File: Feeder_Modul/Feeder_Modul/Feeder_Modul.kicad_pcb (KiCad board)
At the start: 2 copper layers, 156.6 x 125.2 mm, 101 parts, among them J1 Conn_02x01, J101 Conn_02x01, J102 Conn_01x06_Male, J103 Conn_02x01, J104 Conn_02x01, J105 Conn_02x01, J106 WE_629104190121, J107 Conn_02x07_Odd_Even, J108 Conn_02x01, J109 Conn_02x01, SW101 SW_Push, SW102 SW_Push, SW103 SW_Push, SW104 SW_Push, SW105 SW_Push, U1 TPS560430, U101 TPS560430, U102 STM32F105R8Tx, U103 M24C01-WMN, U104 TCST5250, U105 DRV8835, U106 Panasonic_ESE22, U107 SN65HVD230, U108 N20_DC_Motor, U109 N20_DC_Motor, Y101 48MHz

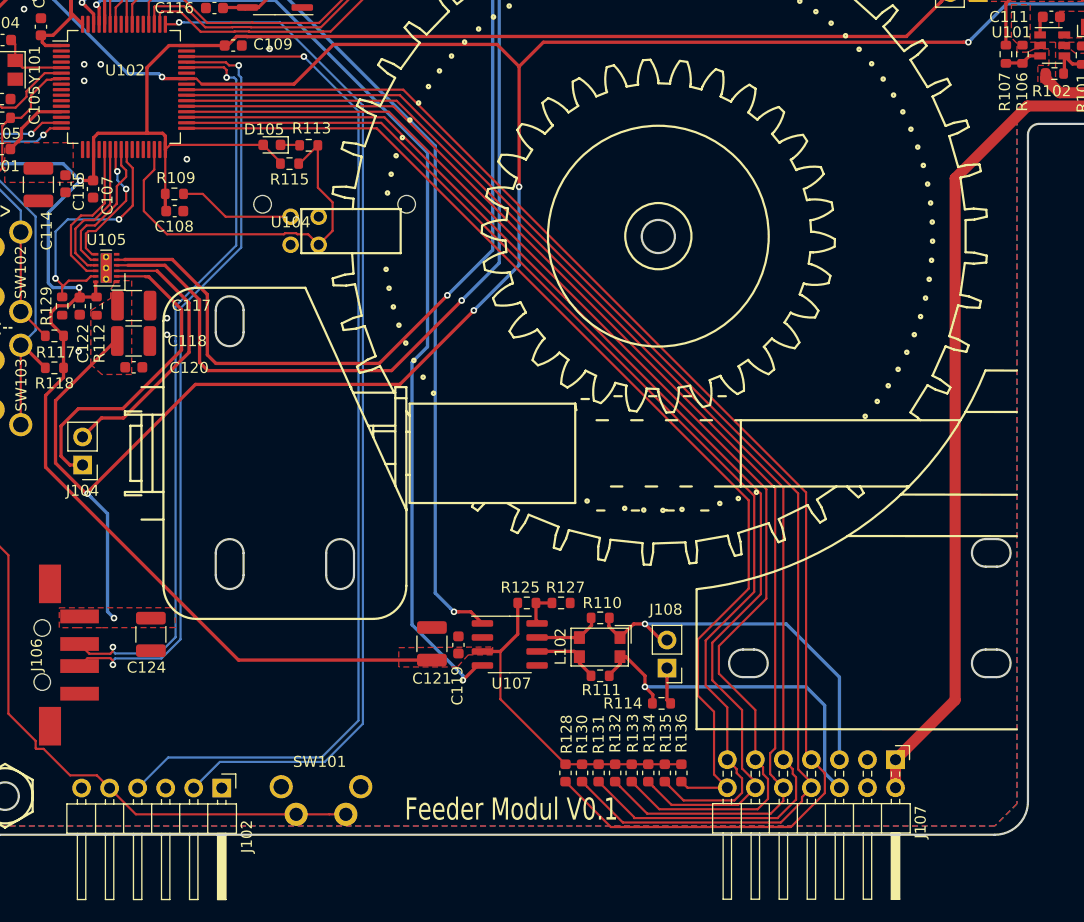
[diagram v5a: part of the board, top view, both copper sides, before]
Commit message: Feeder Rails hinzugefügt
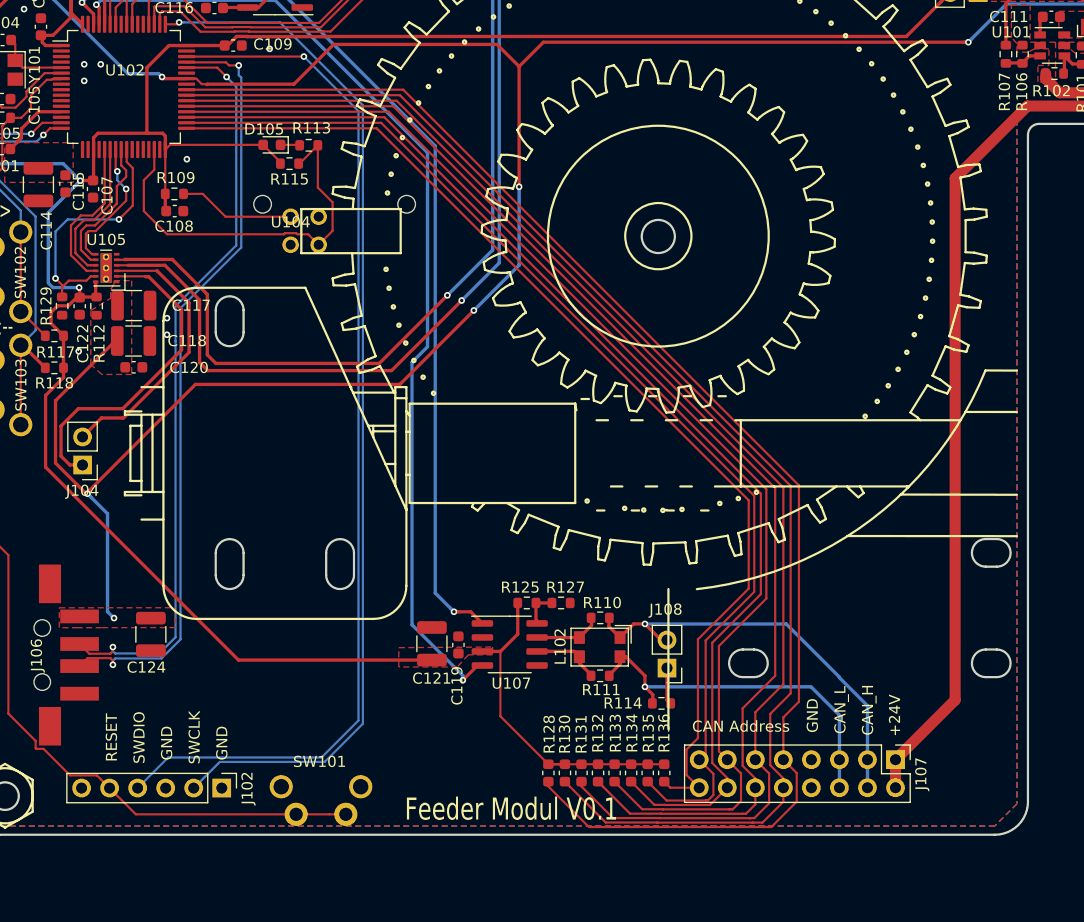
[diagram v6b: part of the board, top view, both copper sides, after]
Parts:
- J102: footprint Connector_PinHeader_2.54mm:PinHeader_1x06_P2.54mm_Horizontal -> Connector_PinHeader_2.54mm:PinHeader_1x06_P2.54mm_Vertical
- J107: footprint Connector_PinHeader_2.54mm:PinHeader_2x07_P2.54mm_Horizontal -> Connector_PinHeader_2.54mm:PinHeader_2x08_P2.54mm_Vertical
- moved R128 1.55 mm to (116.5, 155.2)
- moved R130 1.55 mm to (118.0, 155.2)
- moved R131 1.55 mm to (119.5, 155.2)
- moved R132 1.55 mm to (121.0, 155.2)
- moved R133 1.55 mm to (122.5, 155.2)
- moved R134 1.55 mm to (124.0, 155.2)
- moved R135 1.55 mm to (125.5, 155.2)
- moved R136 1.55 mm to (127.0, 155.2)
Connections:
- J107 pad 10: /ADDR3 -> /ADDR1
- J107 pad 11: /ADDR4 -> /ADDR2
- J107 pad 12: /ADDR5 -> /ADDR3
- J107 pad 13: /ADDR6 -> /ADDR4
- J107 pad 14: /ADDR7 -> /ADDR5
- J107 pad 3: GND -> /CAN1_H
- J107 pad 4: GND -> /CAN1_H
- J107 pad 5: /CAN1_H -> /CAN1_L
- J107 pad 7: /ADDR0 -> GND
- J107 pad 8: /ADDR1 -> GND
- J107 pad 9: /ADDR2 -> /ADDR0
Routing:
- net /CAN1_H: track 34.7 -> 38.3 mm
- net /ADDR5: track 107.4 -> 105.4 mm
- net /ADDR4: track 112.1 -> 110.3 mm
- net /ADDR6: track 103.5 -> 102.0 mm
- net /ADDR7: track 98.3 -> 97.1 mm
- net +3V3: track 350.6 -> 351.5 mm
- net /USB_OTG-: track 68.8 -> 68.0 mm
- net /ADDR2: track 117.3 -> 117.9 mm
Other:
- rule trace_min: 0.1 -> 0.15
- board text added: "+24V"
- board text added: "CAN Address"
- board text added: "CAN_H"
- board text added: "CAN_L"
- board text added: "GND"
- board text added: "RESET"
- board text added: "SWCLK"
- board text added: "SWDIO"

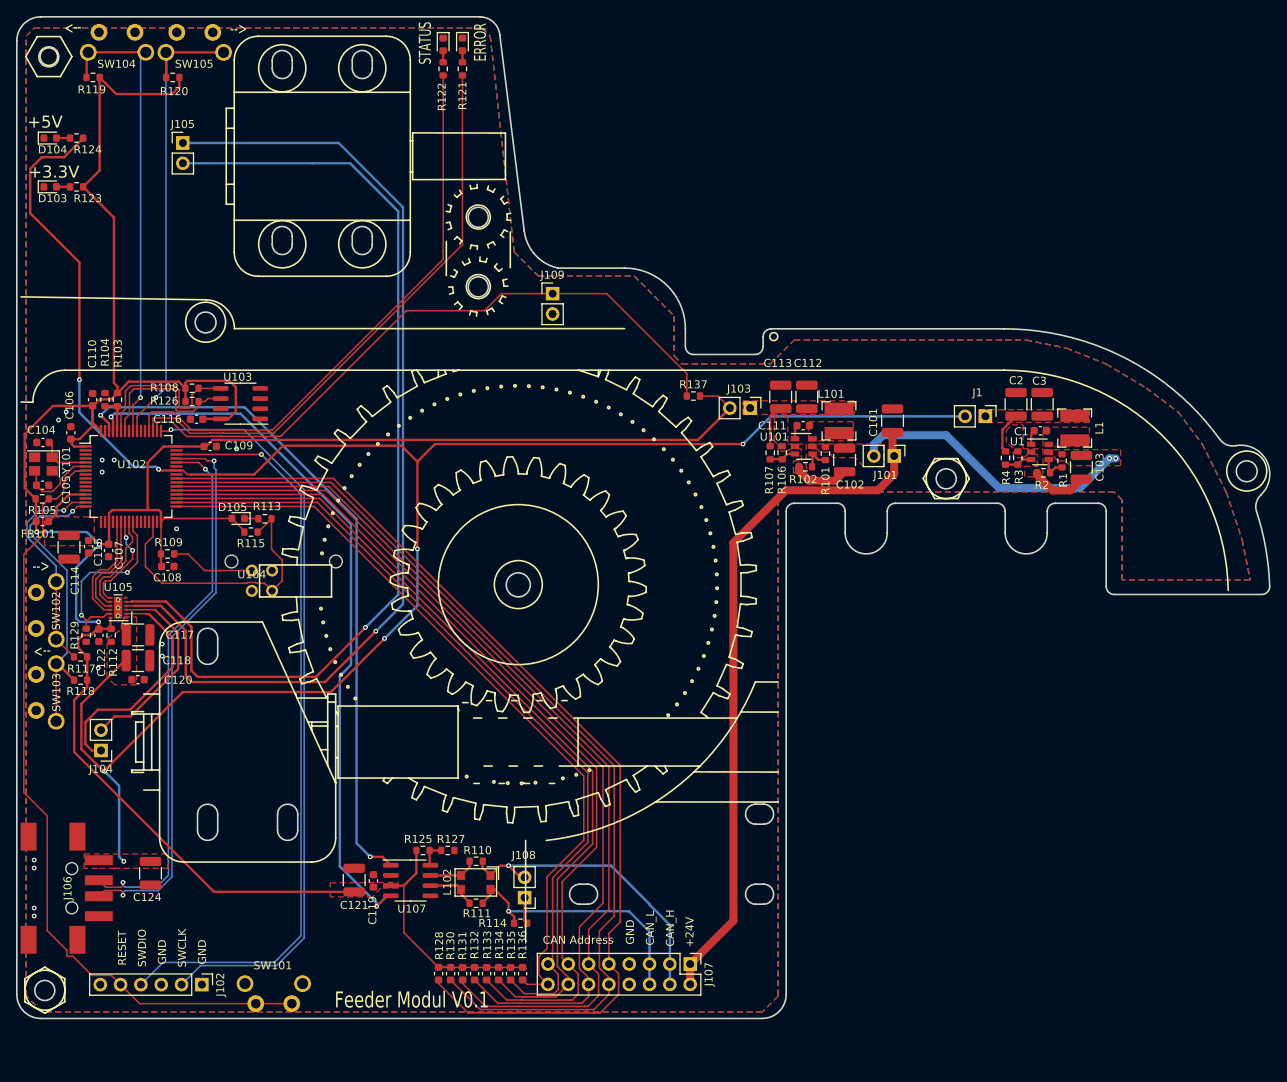
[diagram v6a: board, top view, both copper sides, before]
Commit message: Feeder Rail mit Step files geprüft. Connector am Feeder verschoeben. Halter für Lager muss angepasst werden.
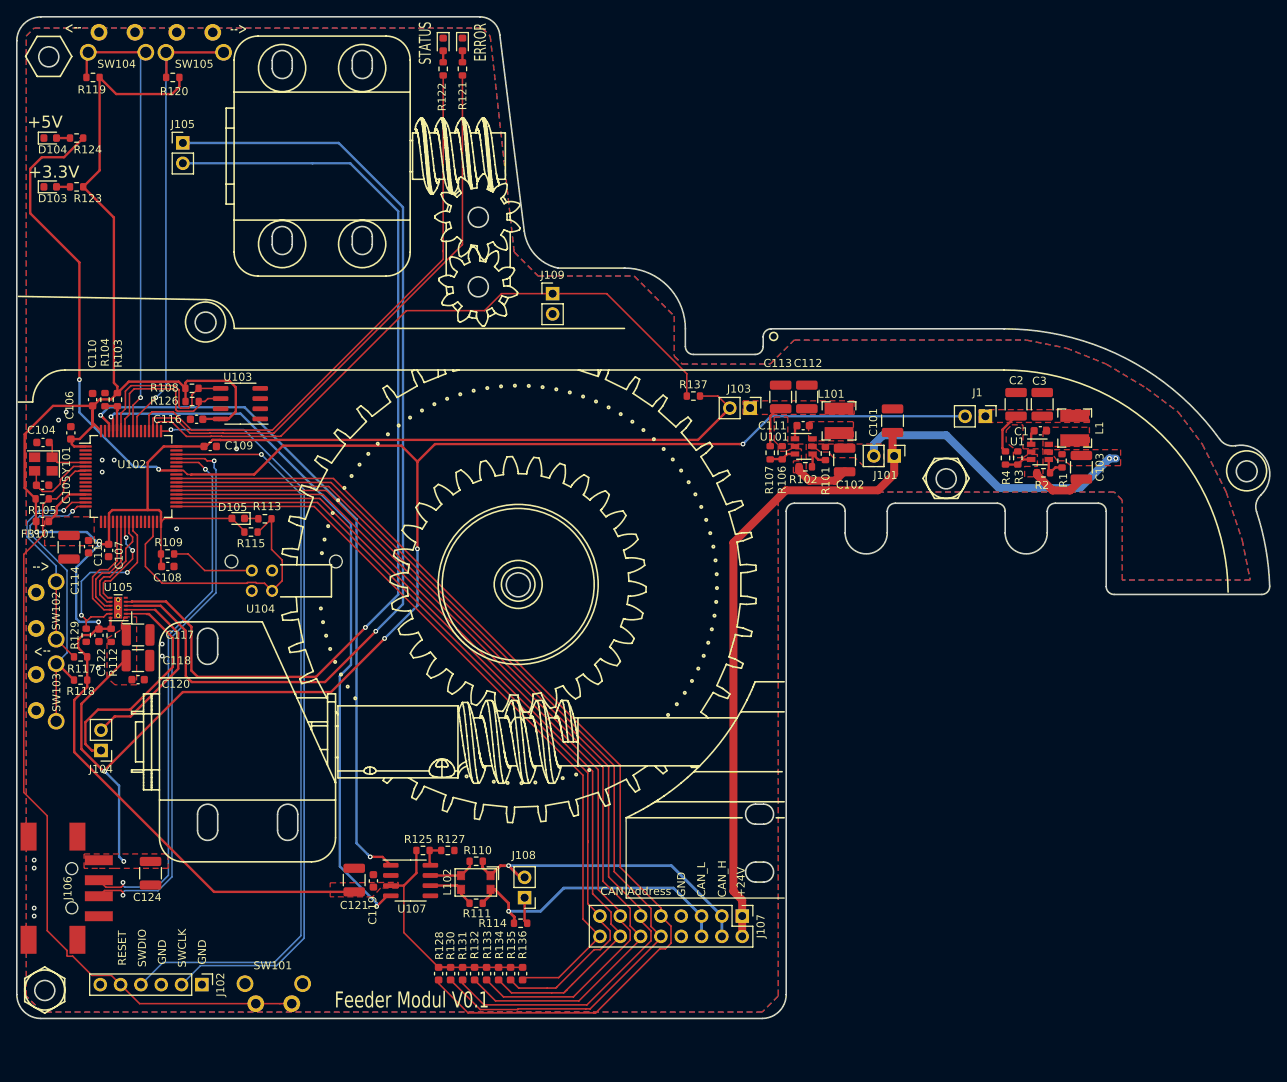
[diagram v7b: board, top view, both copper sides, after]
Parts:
- moved J107 8.85 mm to (154.5, 148.0)
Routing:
- net +24V: track 86.5 -> 78.7 mm
- net /ADDR0: track 125.4 -> 129.8 mm
- net /CAN1_L: track 33.2 -> 37.3 mm
- net /ADDR1: track 121.4 -> 124.9 mm
- net /ADDR2: track 117.9 -> 121.0 mm
- net /ADDR3: track 113.8 -> 116.1 mm
- net /ADDR5: track 105.4 -> 107.4 mm
- net /ADDR4: track 110.3 -> 111.7 mm
- net /CAN1_H: track 38.3 -> 39.4 mm
- net /ADDR6: track 102.0 -> 103.0 mm
- net /ADDR7: track 97.1 -> 97.7 mm
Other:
- outline, holes or cut-outs redrawn

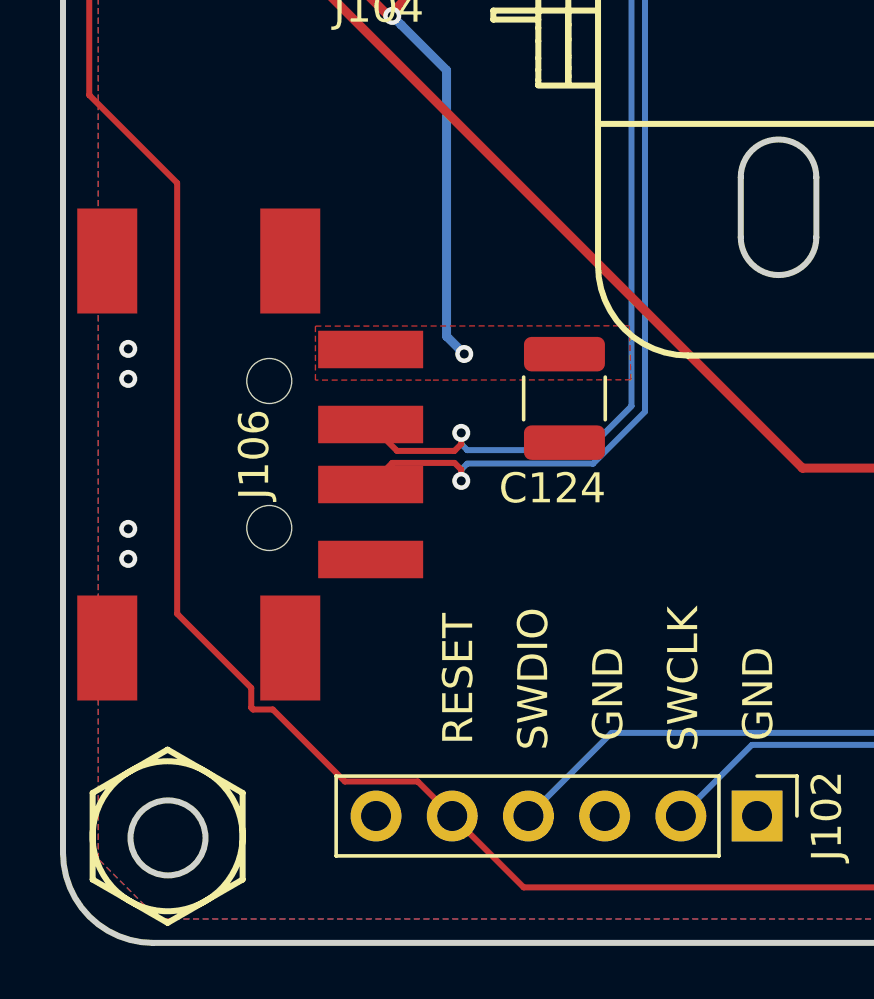
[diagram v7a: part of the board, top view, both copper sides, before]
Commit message: ESD Protection für Feeder Modul USB hinzugefügt, Status LED für Controller Modul hinzugefügt
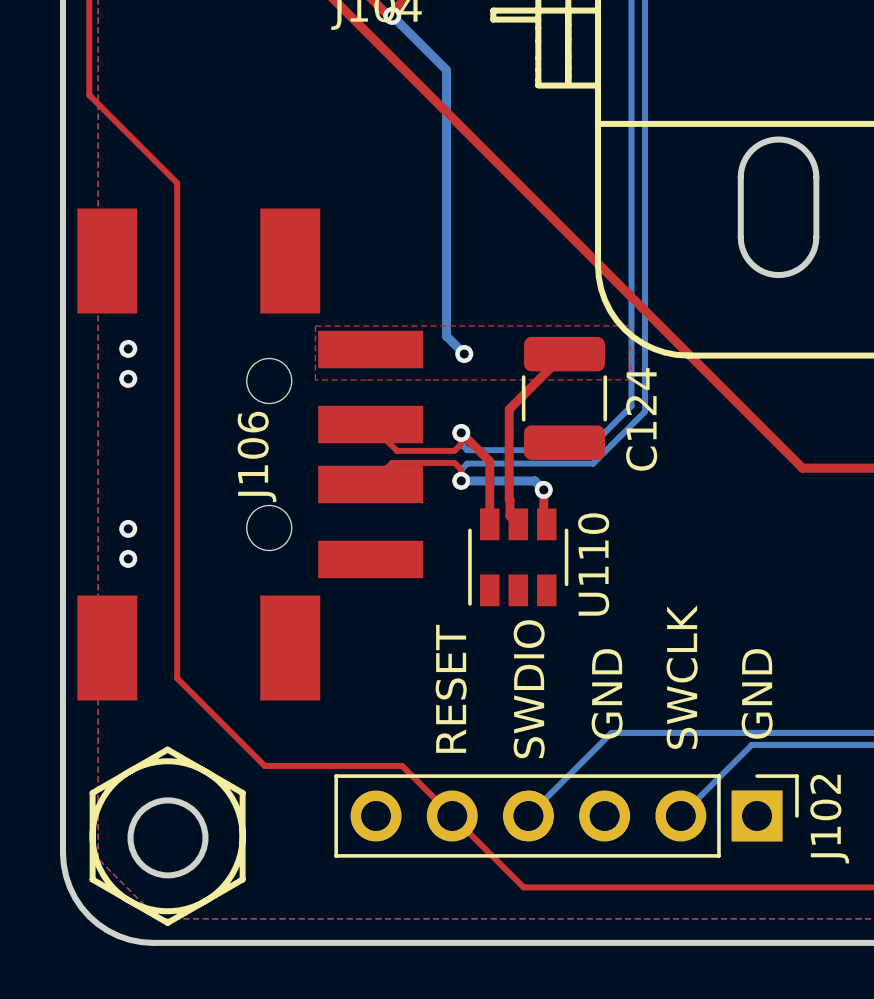
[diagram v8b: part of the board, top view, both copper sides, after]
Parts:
- added U110: SRV05-4, Package_TO_SOT_SMD:SOT-23-6, F.Cu at (79.0, 147.9)
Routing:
- net +5V: track 255.6 -> 262.2 mm
- net /USB_OTG+: track 70.3 -> 74.4 mm, vias 2 -> 3
- net /USB_OTG-: track 68.0 -> 71.4 mm
- net /NRST: track 98.0 -> 98.9 mm
